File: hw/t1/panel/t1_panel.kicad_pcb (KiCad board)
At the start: 4 copper layers, 70.5 x 81 mm, 376 parts, among them J1 SFP edge (INF-8074i), J2 Rosenberger E6S20A-40MT5-Z (H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, U1 DP83TG720S-Q1 (or DP83TC812S-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, U2 STM32G031F6P6, U3 TPS62822DLC, Y1 25MHz CL8pF 2016

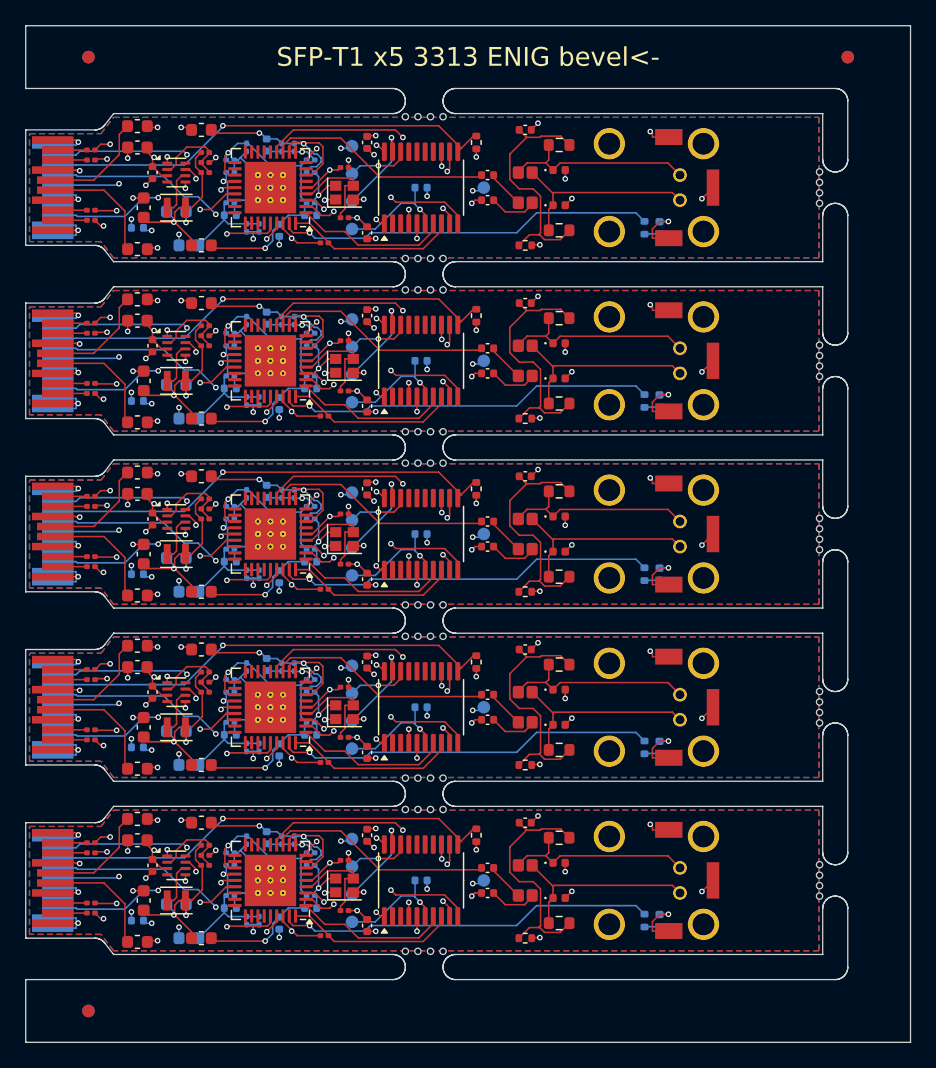
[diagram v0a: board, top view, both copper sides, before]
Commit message: fw: Clause 45 over I2C (mdio-i2c framing: read 0x20|devad, write 5 bytes without it); docs: RJ45 -> RTL8221B, T1S bridge findings
The earlier docs had the C45 write frame wrong. RJ45 moves to the
RTL8221B-VB-CG (100/1000/2500, LCSC stocked; datasheet marked
confidential - noted as the one exception). T1S: no switch chip fits
(all 14x14 TQFP); CrossLink-NX SGMII exists only on csfBGA-121 and its
PCS IP is licensed; Gowin GW5AT-15 is the stocked alternative.

Also: hw/sfpgen.py is the shared generator; netclasses now really reach
the router (patterns in .kicad_pro, rewritten after every Save, routing
in a fresh process, and a guard that refuses an empty class).
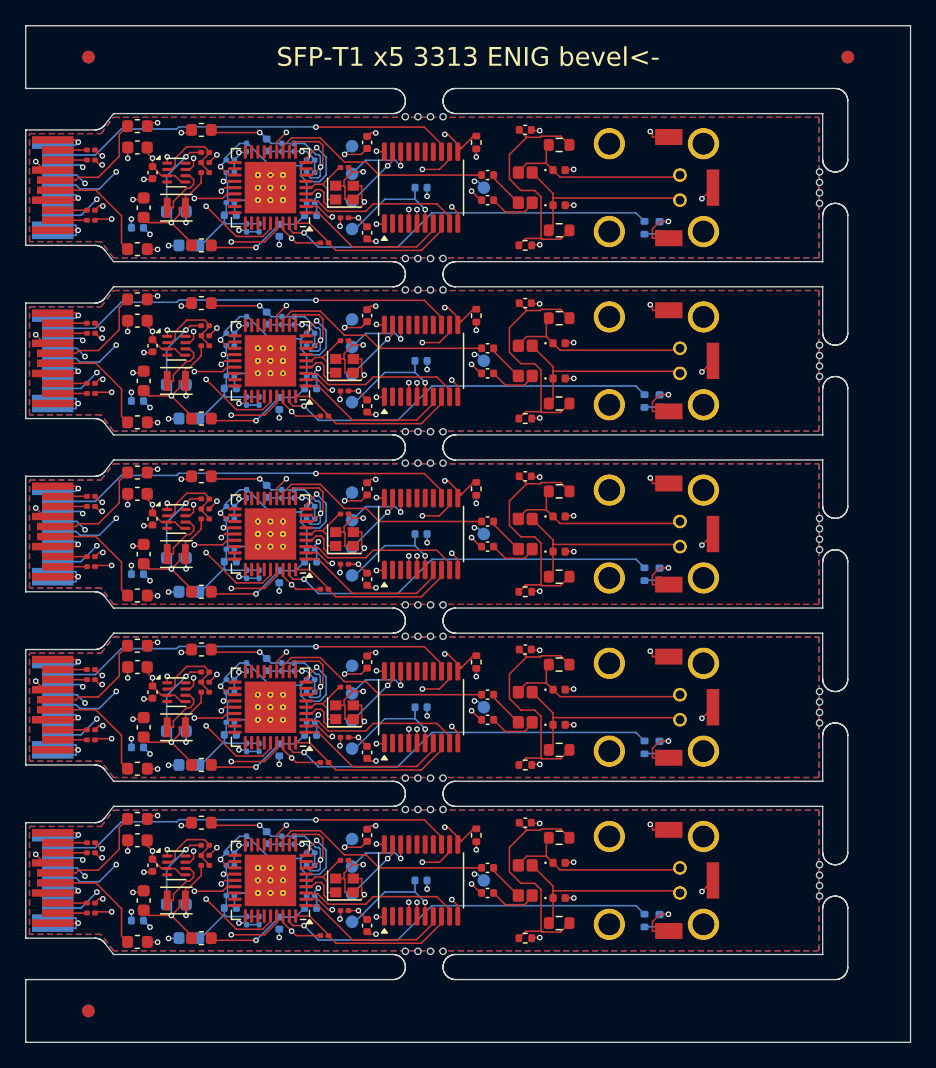
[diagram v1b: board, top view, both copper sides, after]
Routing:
- net Board_2-VDD1P0: track 32.9 -> 28.7 mm
- net Board_1-VDD1P0: track 32.9 -> 28.7 mm
- net Board_4-VDD1P0: track 32.9 -> 28.7 mm
- net Board_0-VDD1P0: track 32.9 -> 28.7 mm
- net Board_3-VDD1P0: track 32.9 -> 28.7 mm
- net Board_0-V1P0_BUCK: track 13.6 -> 17.7 mm, vias 1 -> 2
- net Board_2-V1P0_BUCK: track 13.6 -> 17.7 mm, vias 1 -> 2
- net Board_1-V1P0_BUCK: track 13.6 -> 17.7 mm, vias 1 -> 2
- net Board_4-V1P0_BUCK: track 13.6 -> 17.7 mm, vias 1 -> 2
- net Board_3-V1P0_BUCK: track 13.6 -> 17.7 mm, vias 1 -> 2
- net Board_0-XO: track 8.26 -> 11.5 mm, vias 0 -> 2
- net Board_1-XO: track 8.26 -> 11.5 mm, vias 0 -> 2
- net Board_2-XO: track 8.26 -> 11.5 mm, vias 0 -> 2
- net Board_3-XO: track 8.26 -> 11.5 mm, vias 0 -> 2
- net Board_4-XO: track 8.26 -> 11.5 mm, vias 0 -> 2
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
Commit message: t1: routed DRC-clean with the pairs on F/B only, panel clean
- In2's +3V3 pour goes in after routing: in the DSN it made +3V3 a plane
  net the router never routed, while signals cut the plane up
- SGMII/MDI classes restricted to F and B (use_layer): the router had
  split pairs P-on-B / N-on-In2. U1 pins 12/13 cross over on purpose;
  the PHY corrects MDI polarity itself (datasheet 6.4.7.2)
- placement: Y1 turned 180 so XI/XO face pins 5/4 uncrossed, load caps
  underneath; buck rearranged (divider by FB, input cap under VIN, EN to
  VIN under the package); SWD test points moved off the crystal
- locked pre-routes and escape vias where the router kept failing,
  cap dogbones, then post-route repair: unused escape vias out, open
  links joined before GND stitching, vias into ground islands
- panel: mouse bites 0.1 mm into the board, stitching 1 mm off the long
  edges, bottom label off the edge; panel DRC 0 errors
- ERC 0/0, DRC 0 violations 0 unconnected, pair skew <= 3.2 mm
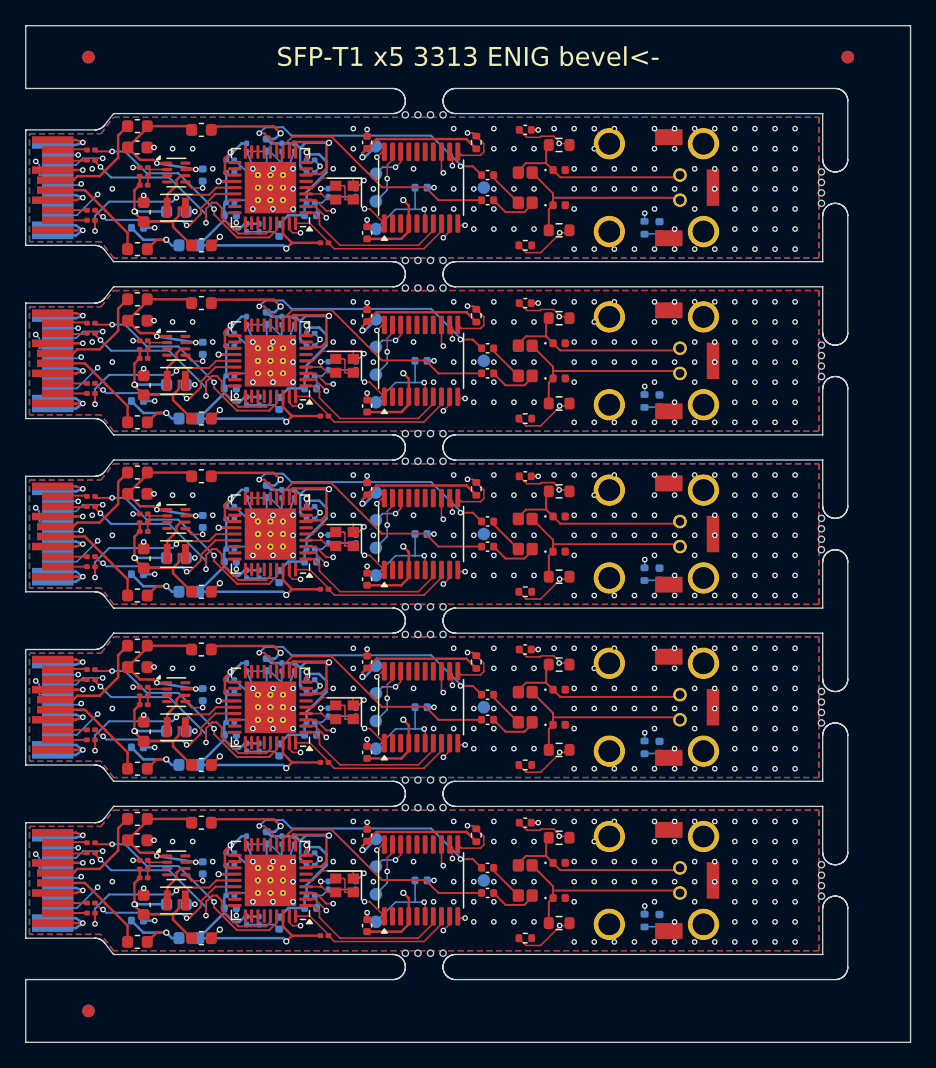
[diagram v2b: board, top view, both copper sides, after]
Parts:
- removed the C24 at (138.7, 45.1)
- removed the C24 at (138.7, 72.7)
- removed the C24 at (138.7, 31.3)
- removed the C24 at (138.7, 86.5)
- removed the C24 at (138.7, 58.9)
- removed the C25 at (138.7, 35.3)
- removed the C25 at (138.7, 76.7)
- removed the C25 at (138.7, 49.1)
- removed the C25 at (138.7, 62.9)
- removed the C25 at (138.7, 90.5)
- removed the C26 at (123.3, 86.9)
- removed the C26 at (123.3, 31.7)
- removed the C26 at (123.3, 45.5)
- removed the C26 at (123.3, 59.3)
- removed the C26 at (123.3, 73.1)
- removed the C27 at (122.7, 89.7)
- removed the C27 at (122.7, 34.5)
- removed the C27 at (122.7, 62.1)
- removed the C27 at (122.7, 48.3)
- removed the C27 at (122.7, 75.9)
- removed the C29 at (127.5, 31.7)
- removed the C29 at (127.5, 45.5)
- removed the C29 at (127.5, 86.9)
- removed the C29 at (127.5, 73.1)
- removed the C29 at (127.5, 59.3)
- removed the R3 at (127.5, 85.3)
- removed the R3 at (127.5, 43.9)
- removed the R3 at (127.5, 57.7)
- removed the R3 at (127.5, 30.1)
- removed the R3 at (127.5, 71.5)
- removed the R4 at (127.5, 58.5)
- removed the R4 at (127.5, 30.9)
- removed the R4 at (127.5, 86.1)
- removed the R4 at (127.5, 44.7)
- removed the R4 at (127.5, 72.3)
- removed the TP1 at (139.2, 57.2)
- removed the TP1 at (139.2, 29.6)
- removed the TP1 at (139.2, 71.0)
- removed the TP1 at (139.2, 43.4)
- removed the TP1 at (139.2, 84.8)
- removed the TP2 at (139.2, 31.8)
- removed the TP2 at (139.2, 45.6)
- removed the TP2 at (139.2, 59.4)
- removed the TP2 at (139.2, 73.2)
- removed the TP2 at (139.2, 87.0)
- removed the TP3 at (139.2, 47.8)
- removed the TP3 at (139.2, 61.6)
- removed the TP3 at (139.2, 34.0)
- removed the TP3 at (139.2, 89.2)
- removed the TP3 at (139.2, 75.4)
- removed the TP4 at (139.2, 63.8)
- removed the TP4 at (139.2, 36.2)
- removed the TP4 at (139.2, 77.6)
- removed the TP4 at (139.2, 50.0)
- removed the TP4 at (139.2, 91.4)
- added C24: 12pF, Capacitor_SMD:C_0201_0603Metric, B.Cu at (139.6, 60.9)
- added C24: 12pF, Capacitor_SMD:C_0201_0603Metric, B.Cu at (139.6, 47.1)
- added C24: 12pF, Capacitor_SMD:C_0201_0603Metric, B.Cu at (139.6, 74.7)
- added C24: 12pF, Capacitor_SMD:C_0201_0603Metric, B.Cu at (139.6, 88.5)
- added C24: 12pF, Capacitor_SMD:C_0201_0603Metric, B.Cu at (139.6, 33.3)
- added C25: 12pF, Capacitor_SMD:C_0201_0603Metric, B.Cu at (137.3, 60.9)
- added C25: 12pF, Capacitor_SMD:C_0201_0603Metric, B.Cu at (137.3, 47.1)
- added C25: 12pF, Capacitor_SMD:C_0201_0603Metric, B.Cu at (137.3, 88.5)
- added C25: 12pF, Capacitor_SMD:C_0201_0603Metric, B.Cu at (137.3, 74.7)
- added C25: 12pF, Capacitor_SMD:C_0201_0603Metric, B.Cu at (137.3, 33.3)
- added C26: 4.7uF, Capacitor_SMD:C_0402_1005Metric, B.Cu at (127.3, 45.7)
- added C26: 4.7uF, Capacitor_SMD:C_0402_1005Metric, B.Cu at (127.3, 31.9)
- added C26: 4.7uF, Capacitor_SMD:C_0402_1005Metric, B.Cu at (127.3, 87.1)
- added C26: 4.7uF, Capacitor_SMD:C_0402_1005Metric, B.Cu at (127.3, 59.5)
- added C26: 4.7uF, Capacitor_SMD:C_0402_1005Metric, B.Cu at (127.3, 73.3)
- added C27: 10uF, Capacitor_SMD:C_0603_1608Metric, F.Cu at (122.7, 48.6)
- added C27: 10uF, Capacitor_SMD:C_0603_1608Metric, F.Cu at (122.7, 34.9)
- added C27: 10uF, Capacitor_SMD:C_0603_1608Metric, F.Cu at (122.7, 76.2)
- added C27: 10uF, Capacitor_SMD:C_0603_1608Metric, F.Cu at (122.7, 90.0)
- added C27: 10uF, Capacitor_SMD:C_0603_1608Metric, F.Cu at (122.7, 62.5)
- added C29: 120pF, Capacitor_SMD:C_0201_0603Metric, F.Cu at (122.7, 87.2)
- added C29: 120pF, Capacitor_SMD:C_0201_0603Metric, F.Cu at (122.7, 73.4)
- added C29: 120pF, Capacitor_SMD:C_0201_0603Metric, F.Cu at (122.7, 59.6)
- added C29: 120pF, Capacitor_SMD:C_0201_0603Metric, F.Cu at (122.7, 45.8)
- added C29: 120pF, Capacitor_SMD:C_0201_0603Metric, F.Cu at (122.7, 32.0)
- added R3: 66.5k 1%, Resistor_SMD:R_0201_0603Metric, F.Cu at (122.7, 60.3)
- added R3: 66.5k 1%, Resistor_SMD:R_0201_0603Metric, F.Cu at (122.7, 46.5)
- added R3: 66.5k 1%, Resistor_SMD:R_0201_0603Metric, F.Cu at (122.7, 87.9)
- added R3: 66.5k 1%, Resistor_SMD:R_0201_0603Metric, F.Cu at (122.7, 74.1)
- added R3: 66.5k 1%, Resistor_SMD:R_0201_0603Metric, F.Cu at (122.7, 32.7)
- added R4: 100k 1%, Resistor_SMD:R_0201_0603Metric, F.Cu at (122.7, 58.9)
- added R4: 100k 1%, Resistor_SMD:R_0201_0603Metric, F.Cu at (122.7, 31.3)
- added R4: 100k 1%, Resistor_SMD:R_0201_0603Metric, F.Cu at (122.7, 72.7)
- added R4: 100k 1%, Resistor_SMD:R_0201_0603Metric, F.Cu at (122.7, 86.5)
- added R4: 100k 1%, Resistor_SMD:R_0201_0603Metric, F.Cu at (122.7, 45.1)
- added TP1: +3V3, TestPoint:TestPoint_Pad_D1.0mm, B.Cu at (141.2, 43.4)
- added TP1: +3V3, TestPoint:TestPoint_Pad_D1.0mm, B.Cu at (141.2, 29.6)
- added TP1: +3V3, TestPoint:TestPoint_Pad_D1.0mm, B.Cu at (141.2, 84.8)
- added TP1: +3V3, TestPoint:TestPoint_Pad_D1.0mm, B.Cu at (141.2, 71.0)
- added TP1: +3V3, TestPoint:TestPoint_Pad_D1.0mm, B.Cu at (141.2, 57.2)
- added TP2: SWDIO, TestPoint:TestPoint_Pad_D1.0mm, B.Cu at (141.2, 73.2)
- added TP2: SWDIO, TestPoint:TestPoint_Pad_D1.0mm, B.Cu at (141.2, 31.8)
- added TP2: SWDIO, TestPoint:TestPoint_Pad_D1.0mm, B.Cu at (141.2, 59.4)
- added TP2: SWDIO, TestPoint:TestPoint_Pad_D1.0mm, B.Cu at (141.2, 45.6)
- added TP2: SWDIO, TestPoint:TestPoint_Pad_D1.0mm, B.Cu at (141.2, 87.0)
- added TP3: SWCLK, TestPoint:TestPoint_Pad_D1.0mm, B.Cu at (141.2, 47.8)
- added TP3: SWCLK, TestPoint:TestPoint_Pad_D1.0mm, B.Cu at (141.2, 75.4)
- added TP3: SWCLK, TestPoint:TestPoint_Pad_D1.0mm, B.Cu at (141.2, 61.6)
- added TP3: SWCLK, TestPoint:TestPoint_Pad_D1.0mm, B.Cu at (141.2, 34.0)
- added TP3: SWCLK, TestPoint:TestPoint_Pad_D1.0mm, B.Cu at (141.2, 89.2)
- added TP4: NRST, TestPoint:TestPoint_Pad_D1.0mm, B.Cu at (141.2, 91.4)
- added TP4: NRST, TestPoint:TestPoint_Pad_D1.0mm, B.Cu at (141.2, 36.2)
- added TP4: NRST, TestPoint:TestPoint_Pad_D1.0mm, B.Cu at (141.2, 50.0)
- added TP4: NRST, TestPoint:TestPoint_Pad_D1.0mm, B.Cu at (141.2, 63.8)
- added TP4: NRST, TestPoint:TestPoint_Pad_D1.0mm, B.Cu at (141.2, 77.6)
- moved KiKit_MB_10_1 0.15 mm to (176.7, 73.0)
- moved KiKit_MB_10_2 0.15 mm to (176.7, 73.9)
- moved KiKit_MB_10_3 0.15 mm to (176.7, 74.7)
- moved KiKit_MB_10_4 0.15 mm to (176.7, 75.5)
- moved KiKit_MB_11_1 0.15 mm to (143.5, 68.5)
- moved KiKit_MB_11_2 0.15 mm to (144.5, 68.5)
- moved KiKit_MB_11_3 0.15 mm to (145.5, 68.5)
- moved KiKit_MB_11_4 0.15 mm to (146.5, 68.5)
- moved KiKit_MB_13_1 0.15 mm to (176.7, 86.8)
- moved KiKit_MB_13_2 0.15 mm to (176.7, 87.7)
- moved KiKit_MB_13_3 0.15 mm to (176.7, 88.5)
- moved KiKit_MB_13_4 0.15 mm to (176.7, 89.3)
- moved KiKit_MB_14_1 0.15 mm to (143.5, 82.3)
- moved KiKit_MB_14_2 0.15 mm to (144.5, 82.3)
- moved KiKit_MB_14_3 0.15 mm to (145.5, 82.3)
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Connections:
- U1 pad 12: Board_3-TRD_P -> Board_3-TRD_M
- U1 pad 13: Board_3-TRD_M -> Board_3-TRD_P
- U1 pad 12: Board_2-TRD_P -> Board_2-TRD_M
- U1 pad 13: Board_2-TRD_M -> Board_2-TRD_P
- U1 pad 12: Board_4-TRD_P -> Board_4-TRD_M
- U1 pad 13: Board_4-TRD_M -> Board_4-TRD_P
- U1 pad 12: Board_1-TRD_P -> Board_1-TRD_M
- U1 pad 13: Board_1-TRD_M -> Board_1-TRD_P
- U1 pad 12: Board_0-TRD_P -> Board_0-TRD_M
- U1 pad 13: Board_0-TRD_M -> Board_0-TRD_P
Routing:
- net Board_4-+3V3: track 13.1 -> 64.0 mm, vias 13 -> 5
- net Board_1-+3V3: track 13.1 -> 64.0 mm, vias 13 -> 5
- net Board_3-+3V3: track 13.1 -> 64.0 mm, vias 13 -> 5
- net Board_2-+3V3: track 13.1 -> 64.0 mm, vias 13 -> 5
- net Board_0-+3V3: track 13.1 -> 64.0 mm, vias 13 -> 5
- net Board_4-TX_FAULT: track 32.7 -> 41.2 mm, vias 1 -> 2
- net Board_3-TX_FAULT: track 32.7 -> 41.2 mm, vias 1 -> 2
- net Board_1-TX_FAULT: track 32.7 -> 41.2 mm, vias 1 -> 2
- net Board_0-TX_FAULT: track 32.7 -> 41.2 mm, vias 1 -> 2
- net Board_2-TX_FAULT: track 32.7 -> 41.2 mm, vias 1 -> 2
- net Board_1-SDA: track 27.8 -> 35.8 mm
- net Board_4-SDA: track 27.8 -> 35.8 mm
- net Board_2-SDA: track 27.8 -> 35.8 mm
- net Board_0-SDA: track 27.8 -> 35.8 mm
- net Board_3-SDA: track 27.8 -> 35.8 mm
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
